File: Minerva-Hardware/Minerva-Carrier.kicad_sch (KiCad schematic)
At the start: 14 parts, among them J11 USB_C_Receptacle_USB2.0, Q2 RQ6E080AJ, U1 BQ25798

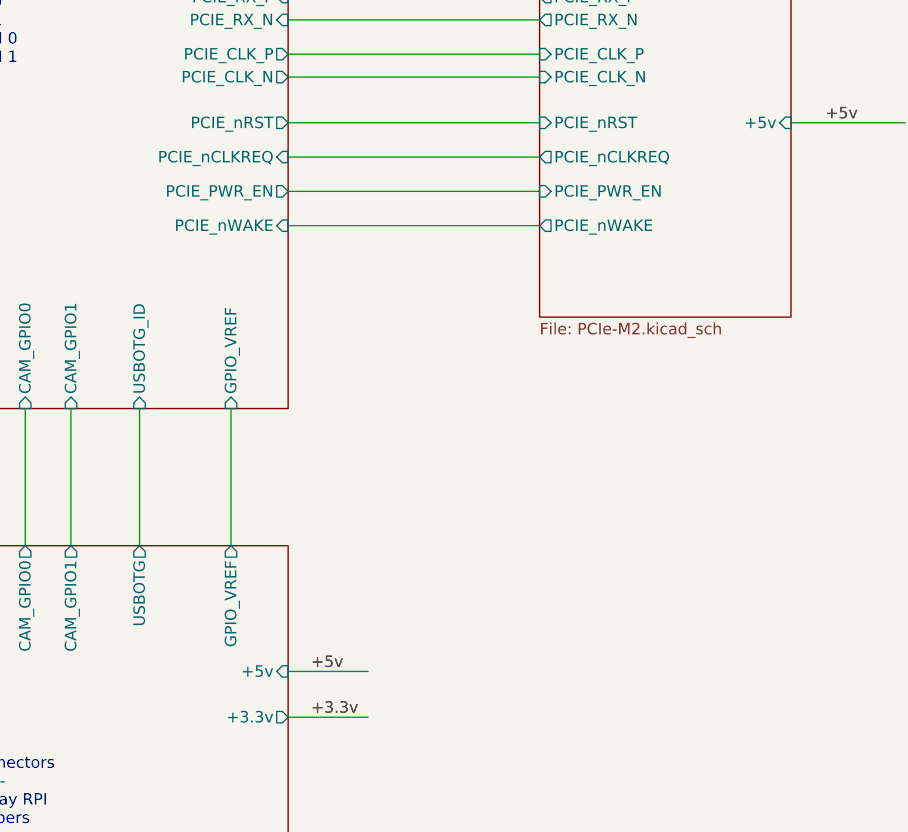
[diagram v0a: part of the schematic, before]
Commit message: Adding MiniPCI-E stuff
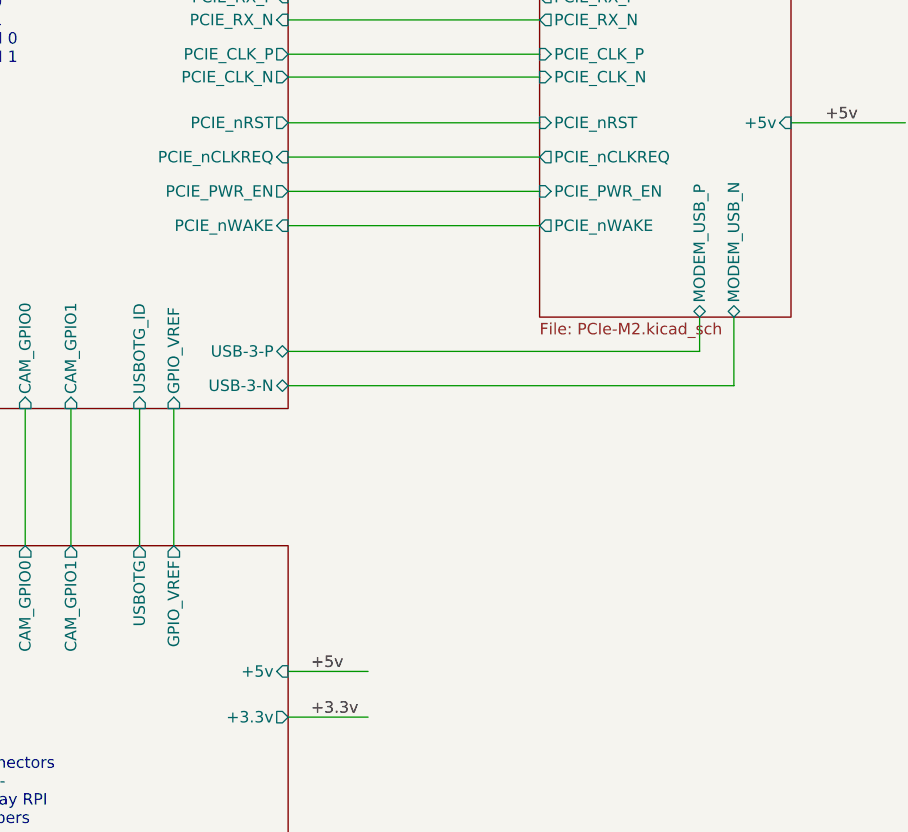
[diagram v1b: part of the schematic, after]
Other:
- sheet CM5_HighSpeed ports: added USB-3-N, USB-3-P; removed none
- sheet PCIe-M2 ports: added MODEM_USB_N, MODEM_USB_P; removed none
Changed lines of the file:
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@@
 	(wire
 		(pts
+			(xy 236.22 93.98) (xy 236.22 86.36)
+		)
+		(stroke
+			(width 0)
+			(type default)
+		)
+	)
+	(wire
+		(pts
 			(xy 186.69 130.81) (xy 195.58 130.81)
 		)
@@
 	(wire
 		(pts
-			(xy 180.34 96.52) (xy 180.34 111.76)
+			(xy 173.99 96.52) (xy 173.99 111.76)
 		)
 		(stroke
@@
 	(wire
 		(pts
+			(xy 232.41 90.17) (xy 232.41 86.36)
+		)
+		(stroke
+			(width 0)
+			(type default)
+		)
+	)
+	(wire
+		(pts
 			(xy 80.01 162.56) (xy 80.01 167.64)
 		)
@@
 	(wire
 		(pts
+			(xy 186.69 90.17) (xy 232.41 90.17)
+		)
+		(stroke
+			(width 0)
+			(type default)
+		)
+	)
+	(wire
+		(pts
 			(xy 69.85 92.71) (xy 69.85 101.6)
 		)
@@
 	(wire
 		(pts
+			(xy 186.69 93.98) (xy 236.22 93.98)
+		)
+		(stroke
+			(width 0)
+			(type default)
+		)
+	)
+	(wire
+		(pts
 			(xy 115.57 50.8) (xy 129.54 50.8)
 		)
@@
 		)
 		(instances
-			(project "CM5IO"
+			(project "Minerva-Carrier"
 				(path "/e63e39d7-6ac0-4ffd-8aa3-1841a4541b55"
 					(reference "H3")
@@
 		)
 		(instances
-			(project "CM5IO"
+			(project "Minerva-Carrier"
 				(path "/e63e39d7-6ac0-4ffd-8aa3-1841a4541b55"
 					(reference "H2")
@@
 		)
 		(instances
-			(project "CM5IO"
+			(project "Minerva-Carrier"
 				(path "/e63e39d7-6ac0-4ffd-8aa3-1841a4541b55"
 					(reference "BT2")
@@
 		)
 		(instances
-			(project "CM5IO"
+			(project "Minerva-Carrier"
 				(path "/e63e39d7-6ac0-4ffd-8aa3-1841a4541b55"
 					(reference "L2")
@@
 		)
 		(instances
-			(project "CM5IO"
+			(project "Minerva-Carrier"
 				(path "/e63e39d7-6ac0-4ffd-8aa3-1841a4541b55"
 					(reference "#PWR031")
@@
 		)
 		(instances
-			(project "CM5IO"
+			(project "Minerva-Carrier"
 				(path "/e63e39d7-6ac0-4ffd-8aa3-1841a4541b55"
 					(reference "R2")
@@
 		)
 		(instances
-			(project "CM5IO"
+			(project "Minerva-Carrier"
 				(path "/e63e39d7-6ac0-4ffd-8aa3-1841a4541b55"
 					(reference "#PWR05")
@@
 		)
 		(instances
-			(project "CM5IO"
+			(project "Minerva-Carrier"
 				(path "/e63e39d7-6ac0-4ffd-8aa3-1841a4541b55"
 					(reference "#PWR032")
@@
 		)
 		(instances
-			(project "CM5IO"
+			(project "Minerva-Carrier"
 				(path "/e63e39d7-6ac0-4ffd-8aa3-1841a4541b55"
 					(reference "C18")
@@
 		)
 		(instances
-			(project "CM5IO"
+			(project "Minerva-Carrier"
 				(path "/e63e39d7-6ac0-4ffd-8aa3-1841a4541b55"
 					(reference "D4")
@@
 		)
 		(instances
-			(project "CM5IO"
+			(project "Minerva-Carrier"
 				(path "/e63e39d7-6ac0-4ffd-8aa3-1841a4541b55"
 					(reference "#PWR03")
@@
 		)
 		(instances
-			(project "CM5IO"
+			(project "Minerva-Carrier"
 				(path "/e63e39d7-6ac0-4ffd-8aa3-1841a4541b55"
 					(reference "C5")
@@
 		)
 		(instances
-			(project "CM5IO"
+			(project "Minerva-Carrier"
 				(path "/e63e39d7-6ac0-4ffd-8aa3-1841a4541b55"
 					(reference "#PWR04")
@@
 		)
 		(instances
-			(project "CM5IO"
+			(project "Minerva-Carrier"
 				(path "/e63e39d7-6ac0-4ffd-8aa3-1841a4541b55"
 					(reference "J11")
@@
 		)
 		(instances
-			(project "CM5IO"
+			(project "Minerva-Carrier"
 				(path "/e63e39d7-6ac0-4ffd-8aa3-1841a4541b55"
 					(reference "R9")
@@
 		)
 		(instances
-			(project "CM5IO"
+			(project "Minerva-Carrier"
 				(path "/e63e39d7-6ac0-4ffd-8aa3-1841a4541b55"
 					(reference "C1")
@@
 		)
 		(instances
-			(project "CM5IO"
+			(project "Minerva-Carrier"
 				(path "/e63e39d7-6ac0-4ffd-8aa3-1841a4541b55"
 					(reference "U1")
@@
 		)
 		(instances
-			(project "CM5IO"
+			(project "Minerva-Carrier"
 				(path "/e63e39d7-6ac0-4ffd-8aa3-1841a4541b55"
 					(reference "C9")
@@
 		)
 		(instances
-			(project "CM5IO"
+			(project "Minerva-Carrier"
 				(path "/e63e39d7-6ac0-4ffd-8aa3-1841a4541b55"
 					(reference "#PWR02")
@@
 		)
 		(instances
-			(project "CM5IO"
+			(project "Minerva-Carrier"
 				(path "/e63e39d7-6ac0-4ffd-8aa3-1841a4541b55"
 					(reference "Q2")
@@
 		)
 		(instances
-			(project "CM5IO"
+			(project "Minerva-Carrier"
 				(path "/e63e39d7-6ac0-4ffd-8aa3-1841a4541b55"
 					(reference "#PWR013")
@@
 		)
 		(pin "GPIO_VREF" output
-			(at 180.34 111.76 90)
+			(at 173.99 111.76 90)
 			(effects
 				(font
@@
 		)
 		(pin "GPIO_VREF" input
-			(at 180.34 96.52 270)
+			(at 173.99 96.52 270)
 			(effects
 				(font
@@
 			)
 		)
+		(pin "USB-3-P" bidirectional
+			(at 186.69 90.17 0)
+			(effects
+				(font
+					(size 1.27 1.27)
+				)
+				(justify right)
+			)
+		)
+		(pin "USB-3-N" bidirectional
+			(at 186.69 93.98 0)
+			(effects
+				(font
+					(size 1.27 1.27)
+				)
+				(justify right)
+			)
+		)
 		(instances
 			(project "Minerva-Carrier"
@@
 			(effects
 				(font
+					(size 1.27 1.27)
+				)
+				(justify left)
+			)
+		)
+		(pin "MODEM_USB_N" bidirectional
+			(at 236.22 86.36 270)
+			(effects
+				(font
+					(size 1.27 1.27)
+				)
+				(justify left)
+			)
+		)
+		(pin "MODEM_USB_P" bidirectional
+			(at 232.41 86.36 270)
+			(effects
+				(font
